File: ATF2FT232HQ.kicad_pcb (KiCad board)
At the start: 2 copper layers, 29.1 x 42.5 mm, 15 parts, among them J1 FT232HQ-Shield, J2 JTAG, SW1 SW_SPST, U1 ATF1504AS-10JU44, U2 MAX662A

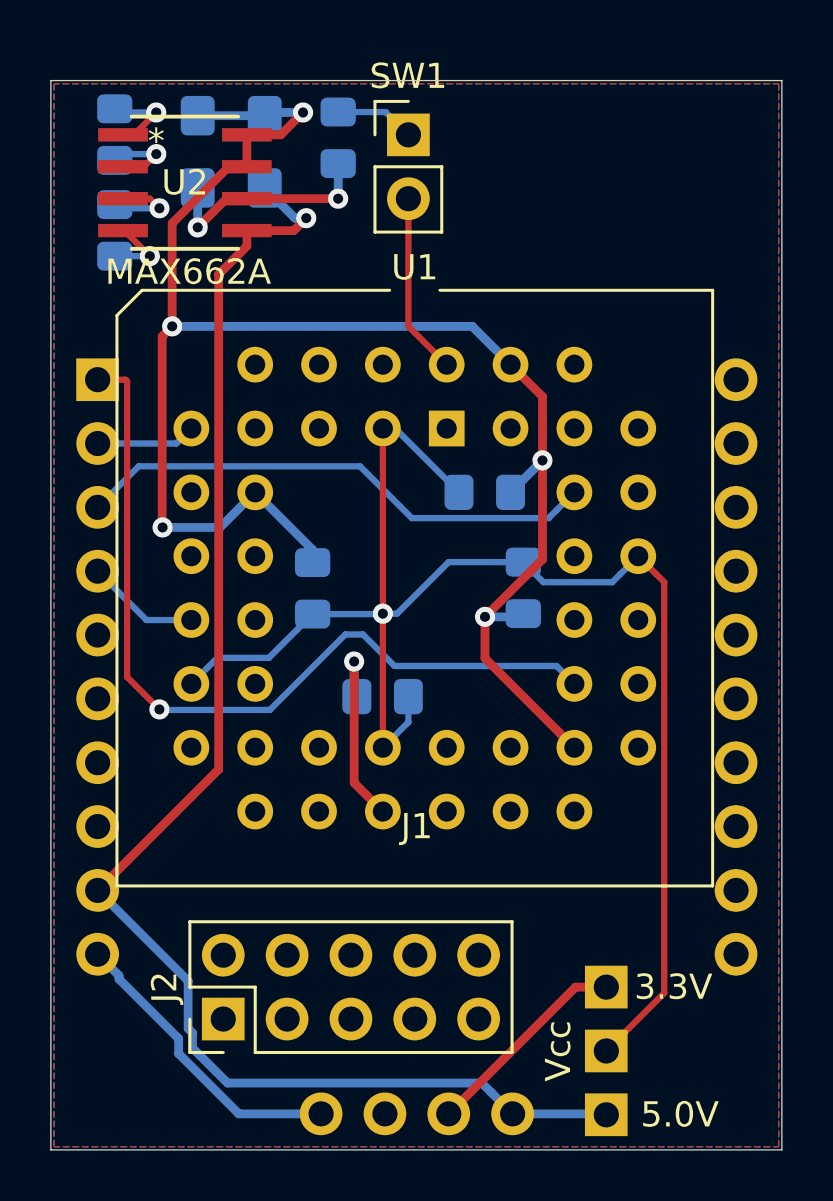
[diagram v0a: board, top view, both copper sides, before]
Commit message: First routing completed.
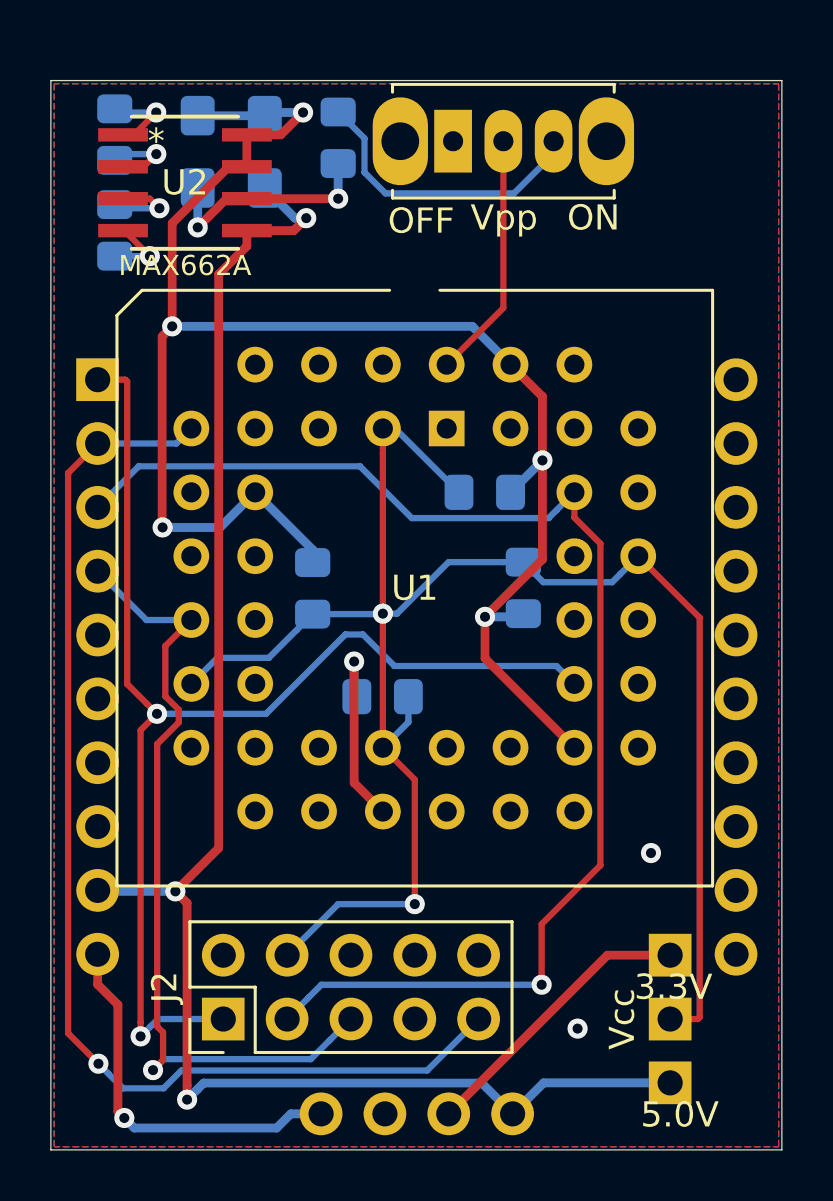
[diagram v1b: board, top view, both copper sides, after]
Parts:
- R1: value R -> 2k2
- SW1: value SW_SPST -> Vpp; footprint Connector_PinHeader_2.54mm:PinHeader_1x02_P2.54mm_Vertical -> Button_Switch_THT:SW_Slide_1P2T_CK_OS102011MS2Q
- moved JP1 2.84 mm to (180.0, 101.6)
- moved SW1 1.80 mm to (171.3, 64.1)
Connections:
- J2 pad 1: Net-(J2-Pad1) -> TCK
- J2 pad 10: Net-(J2-Pad10) -> GND
- J2 pad 2: Net-(J2-Pad2) -> GND
- J2 pad 3: Net-(J2-Pad3) -> TDO
- J2 pad 4: Net-(J2-Pad4) -> VCC
- J2 pad 5: Net-(J2-Pad5) -> TMS
- J2 pad 9: Net-(J2-Pad9) -> TDI
- SW1 pad 1: Net-(R1-Pad2) -> Net-(SW1-Pad1)
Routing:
- net TDI: track 3.98 -> 46.3 mm, vias 0 -> 1
- net TDO: track 20.9 -> 52.6 mm, vias 0 -> 1
- net TMS: track 4.53 -> 32.4 mm, vias 0 -> 1
- net TCK: track 33.4 -> 50.3 mm, vias 1 -> 2
- net VCC: track 60.9 -> 73.0 mm, vias 1 -> 2
- net Net-(R1-Pad2): track 3.17 -> 11.9 mm
- net +5V: track 58.8 -> 64.3 mm, vias 1 -> 3
- net GND: track 87.8 -> 91.0 mm, vias 6 -> 9
- net +3V3: track 8.36 -> 11.4 mm
- net Net-(SW1-Pad2): track 7.24 -> 9.82 mm
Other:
- board text added: "OFF"
- board text added: "ON"

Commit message: Moved components to the top.
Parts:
- C5, C6, C7, C8, R1: moved to F.Cu
- SW1: footprint Button_Switch_THT:SW_Slide_1P2T_CK_OS102011MS2Q -> Connector_PinHeader_2.54mm:PinHeader_1x03_P2.54mm_Vertical
- moved SW1 11.9 mm to (182.5, 68.3), turned to 180 degrees
- moved C7 7.37 mm to (168.5, 64.5)
- moved C8 7.24 mm to (171.1, 64.5)
- moved R1 6.83 mm to (173.5, 65.2)
- moved U2 2.54 mm to (163.2, 65.8)
- moved C5 0.13 mm to (158.0, 63.9)
- moved C6 0.13 mm to (158.0, 67.7)
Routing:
- net GND: track 91.0 -> 77.6 mm, vias 9 -> 8
- net Net-(SW1-Pad2): track 9.82 -> 18.5 mm, vias 0 -> 1
- net Net-(R1-Pad2): track 11.9 -> 9.38 mm
- net +5V: track 64.3 -> 66.7 mm, vias 3 -> 2
- net Net-(C6-Pad1): track 3.44 -> 2.84 mm, vias 1 -> 0
- net Net-(C5-Pad2): track 3.29 -> 2.85 mm, vias 1 -> 0
- net Net-(C6-Pad2): track 2.88 -> 3.16 mm, vias 1 -> 0
- net Net-(C5-Pad1): track 3.40 -> 3.17 mm, vias 1 -> 0
- net +12V: track 9.03 -> 9.07 mm, vias 2 -> 0
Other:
- board text added: "3.3"
- board text added: "5.0"
- board text added: "GND"
- board text added: "TCK"
- board text added: "TDI"
- board text added: "TDO"
- board text added: "TMS"
- board text added: "VCC"
- board text removed: "3.3V"
- board text removed: "5.0V"

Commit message: Labeled and tagged.
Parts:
- added G***: LOGO, Logo:bigby2, B.Cu at (157.5, 64.3)
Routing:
- net GND: track 77.6 -> 74.9 mm
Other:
- board text added: "ATF1504-FT232HQ Shield Rev.1 2019"
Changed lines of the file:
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@@
   (general
     (thickness 1.6)
-    (drawings 15)
-    (tracks 177)
+    (drawings 16)
+    (tracks 176)
     (zones 0)
-    (modules 15)
+    (modules 16)
     (nets 66)
   )
@@
     (add_net GND)
   )
+  (module Logo:bigby2 (layer B.Cu)
+    (at 157.48 64.262 180)
+    (fp_text reference G*** (at 0 0 180) (layer B.SilkS) hide
+      (effects (font (size 1.524 1.524) (thickness 0.3)) (justify mirror))
+    )
+    (fp_text value LOGO (at 0.75 0 180) (layer B.SilkS) hide
+      (effects (font (size 1.524 1.524) (thickness 0.3)) (justify mirror))
+    )
+    (fp_poly (pts (xy -0.011485 1.728467) (xy 0.113732 1.717124) (xy 0.194843 1.687923) (xy 0.241542 1.632439)
+      (xy 0.263521 1.542246) (xy 0.270474 1.408921) (xy 0.271308 1.328994) (xy 0.273257 1.04049)
+      (xy 0.168379 0.956808) (xy 0.105032 0.892095) (xy 0.067481 0.826879) (xy 0.062385 0.77734)
+      (xy 0.087312 0.759744) (xy 0.127711 0.756134) (xy 0.215607 0.74839) (xy 0.335236 0.737898)
+      (xy 0.394892 0.732679) (xy 0.531508 0.719487) (xy 0.621502 0.704831) (xy 0.681588 0.682684)
+      (xy 0.728481 0.647018) (xy 0.775892 0.595287) (xy 0.854874 0.518356) (xy 0.944952 0.451548)
+      (xy 1.029404 0.405121) (xy 1.09151 0.389332) (xy 1.105316 0.393209) (xy 1.115338 0.429014)
+      (xy 1.124376 0.514977) (xy 1.131371 0.637757) (xy 1.13502 0.76718) (xy 1.139106 0.928835)
+      (xy 1.146403 1.038611) (xy 1.158673 1.108111) (xy 1.177674 1.14894) (xy 1.195579 1.166425)
+      (xy 1.29101 1.202114) (xy 1.400648 1.196807) (xy 1.475118 1.16372) (xy 1.488952 1.150785)
+      (xy 1.500416 1.130319) (xy 1.509731 1.096728) (xy 1.517116 1.04442) (xy 1.522788 0.9678)
+      (xy 1.526969 0.861275) (xy 1.529876 0.71925) (xy 1.531729 0.536133) (xy 1.532746 0.306329)
+      (xy 1.533148 0.024245) (xy 1.533153 -0.315712) (xy 1.533153 -0.317844) (xy 1.532922 -0.658253)
+      (xy 1.532326 -0.940751) (xy 1.531144 -1.170927) (xy 1.529156 -1.354371) (xy 1.52614 -1.496672)
+      (xy 1.521875 -1.603419) (xy 1.516141 -1.680201) (xy 1.508718 -1.732606) (xy 1.499384 -1.766226)
+      (xy 1.487919 -1.786647) (xy 1.474647 -1.799064) (xy 1.376472 -1.836684) (xy 1.265456 -1.831892)
+      (xy 1.193094 -1.799607) (xy 1.175112 -1.781995) (xy 1.1613 -1.753588) (xy 1.151101 -1.706603)
+      (xy 1.14396 -1.633257) (xy 1.139323 -1.525767) (xy 1.136633 -1.37635) (xy 1.135335 -1.177223)
+      (xy 1.134934 -0.984675) (xy 1.134065 -0.211637) (xy 0.979782 -0.062148) (xy 0.901816 0.017658)
+      (xy 0.846345 0.082572) (xy 0.825499 0.118224) (xy 0.799146 0.148761) (xy 0.732681 0.189721)
+      (xy 0.696557 0.207251) (xy 0.613805 0.241662) (xy 0.55975 0.248672) (xy 0.505771 0.22821)
+      (xy 0.468235 0.206692) (xy 0.396192 0.15478) (xy 0.300546 0.073678) (xy 0.201272 -0.019618)
+      (xy 0.19561 -0.025259) (xy 0.022365 -0.198504) (xy 0.14612 -0.3024) (xy 0.221538 -0.372494)
+      (xy 0.258266 -0.434497) (xy 0.270015 -0.516179) (xy 0.270766 -0.55481) (xy 0.276486 -0.647599)
+      (xy 0.301118 -0.711947) (xy 0.35795 -0.773886) (xy 0.401734 -0.811372) (xy 0.531811 -0.919421)
+      (xy 0.518782 -1.176497) (xy 0.505754 -1.433573) (xy 0.798146 -1.702035) (xy 0.735253 -1.779705)
+      (xy 0.694397 -1.821324) (xy 0.644378 -1.844797) (xy 0.566817 -1.855141) (xy 0.450638 -1.857375)
+      (xy 0.297496 -1.851301) (xy 0.197085 -1.826154) (xy 0.139611 -1.771549) (xy 0.11528 -1.6771)
+      (xy 0.114298 -1.532418) (xy 0.115741 -1.502222) (xy 0.117859 -1.346848) (xy 0.100457 -1.238092)
+      (xy 0.056678 -1.160347) (xy -0.020335 -1.098007) (xy -0.075669 -1.066562) (xy -0.152049 -1.029637)
+      (xy -0.205195 -1.023113) (xy -0.267621 -1.046992) (xy -0.305332 -1.066562) (xy -0.402294 -1.127059)
+      (xy -0.462465 -1.194861) (xy -0.492699 -1.285576) (xy -0.499855 -1.414809) (xy -0.496742 -1.502222)
+      (xy -0.492373 -1.63025) (xy -0.497412 -1.711576) (xy -0.514532 -1.762642) (xy -0.544891 -1.798527)
+      (xy -0.615745 -1.832954) (xy -0.725524 -1.856221) (xy -0.850294 -1.866168) (xy -0.966123 -1.860635)
+      (xy -1.037737 -1.842993) (xy -1.107556 -1.793603) (xy -1.139614 -1.752578) (xy -1.150671 -1.711431)
+      (xy -1.131349 -1.666613) (xy -1.0735 -1.604152) (xy -1.029397 -1.563569) (xy -0.886666 -1.435314)
+      (xy -0.899789 -1.176378) (xy -0.912912 -0.917443) (xy -0.793004 -0.821082) (xy -0.704937 -0.7312)
+      (xy -0.659639 -0.643046) (xy -0.661706 -0.568683) (xy -0.685037 -0.537748) (xy -0.742867 -0.520353)
+      (xy -0.789634 -0.537546) (xy -0.90009 -0.569107) (xy -1.015232 -0.559689) (xy -1.107263 -0.511844)
+      (xy -1.11125 -0.508) (xy -1.157841 -0.451438) (xy -1.17475 -0.413565) (xy -1.200203 -0.379535)
+      (xy -1.262383 -0.337448) (xy -1.271377 -0.332663) (xy -1.350006 -0.274409) (xy -1.403716 -0.204314)
+      (xy -1.403829 -0.204068) (xy -1.454851 -0.13485) (xy -1.533039 -0.068093) (xy -1.545327 -0.06013)
+      (xy -1.613576 -0.004066) (xy -1.649417 0.052464) (xy -1.651 0.0635) (xy -1.649159 0.067395)
+      (xy -1.237666 0.067395) (xy -1.21517 0.004673) (xy -1.141624 -0.048336) (xy -1.062668 -0.107176)
+      (xy -1.008449 -0.17852) (xy -1.008424 -0.178574) (xy -0.954971 -0.24511) (xy -0.867178 -0.312438)
+      (xy -0.771491 -0.362989) (xy -0.705807 -0.379596) (xy -0.656443 -0.364494) (xy -0.578184 -0.324688)
+      (xy -0.53912 -0.301226) (xy -0.464733 -0.251149) (xy -0.419317 -0.214564) (xy -0.41275 -0.205286)
+      (xy -0.43488 -0.171195) (xy -0.492715 -0.108258) (xy -0.57342 -0.028572) (xy -0.664165 0.055766)
+      (xy -0.752115 0.132658) (xy -0.824438 0.190008) (xy -0.850696 0.207554) (xy -0.913247 0.241447)
+      (xy -0.961408 0.250082) (xy -1.020442 0.232418) (xy -1.094894 0.197474) (xy -1.197469 0.132211)
+      (xy -1.237666 0.067395) (xy -1.649159 0.067395) (xy -1.625844 0.116715) (xy -1.563551 0.174994)
+      (xy -1.545327 0.187131) (xy -1.465273 0.251521) (xy -1.407673 0.323668) (xy -1.40292 0.333063)
+      (xy -1.349062 0.406423) (xy -1.293916 0.446614) (xy -1.227193 0.497303) (xy -1.167951 0.573103)
+      (xy -1.167761 0.573433) (xy -1.09407 0.659684) (xy -0.986869 0.710192) (xy -0.834991 0.729664)
+      (xy -0.795652 0.730251) (xy -0.620132 0.738307) (xy -0.505713 0.762691) (xy -0.452045 0.803723)
+      (xy -0.458779 0.861724) (xy -0.525567 0.937016) (xy -0.54938 0.956808) (xy -0.654258 1.04049)
+      (xy -0.652309 1.328994) (xy -0.649069 1.485493) (xy -0.635357 1.594901) (xy -0.601479 1.665643)
+      (xy -0.537743 1.706143) (xy -0.434455 1.724827) (xy -0.281922 1.730119) (xy -0.1905 1.730375)
+      (xy -0.011485 1.728467)) (layer B.Cu) (width 0.01))
+  )
   (module max662:MAX662ACSA&plus_ (layer F.Cu)
     (at 163.195 65.786)
@@
       (rotate (xyz 0 0 0))
     )
+  )
+  (gr_text "ATF1504-FT232HQ\nShield Rev.1 2019" (at 166.624 64.008) (layer B.Cu)
+    (effects (font (size 1 1) (thickness 0.2)) (justify mirror))
   )
   (gr_text TDI (at 172.339 101.092) (layer F.SilkS)
@@
   (segment (start 161.995201 92.258799) (end 161.995201 71.971299) (width 0.35) (layer F.Cu) (net 9))
   (segment (start 161.995201 71.971299) (end 165.6588 68.3077) (width 0.35) (layer F.Cu) (net 9))
-  (segment (start 163.83 63.119) (end 161.163 63.119) (width 0.35) (layer B.Cu) (net 10))
   (via (at 160.147 71.501) (size 0.8) (drill 0.4) (layers F.Cu B.Cu) (net 10))
   (segment (start 172.085 71.501) (end 173.609 73.025) (width 0.35) (layer B.Cu) (net 10))

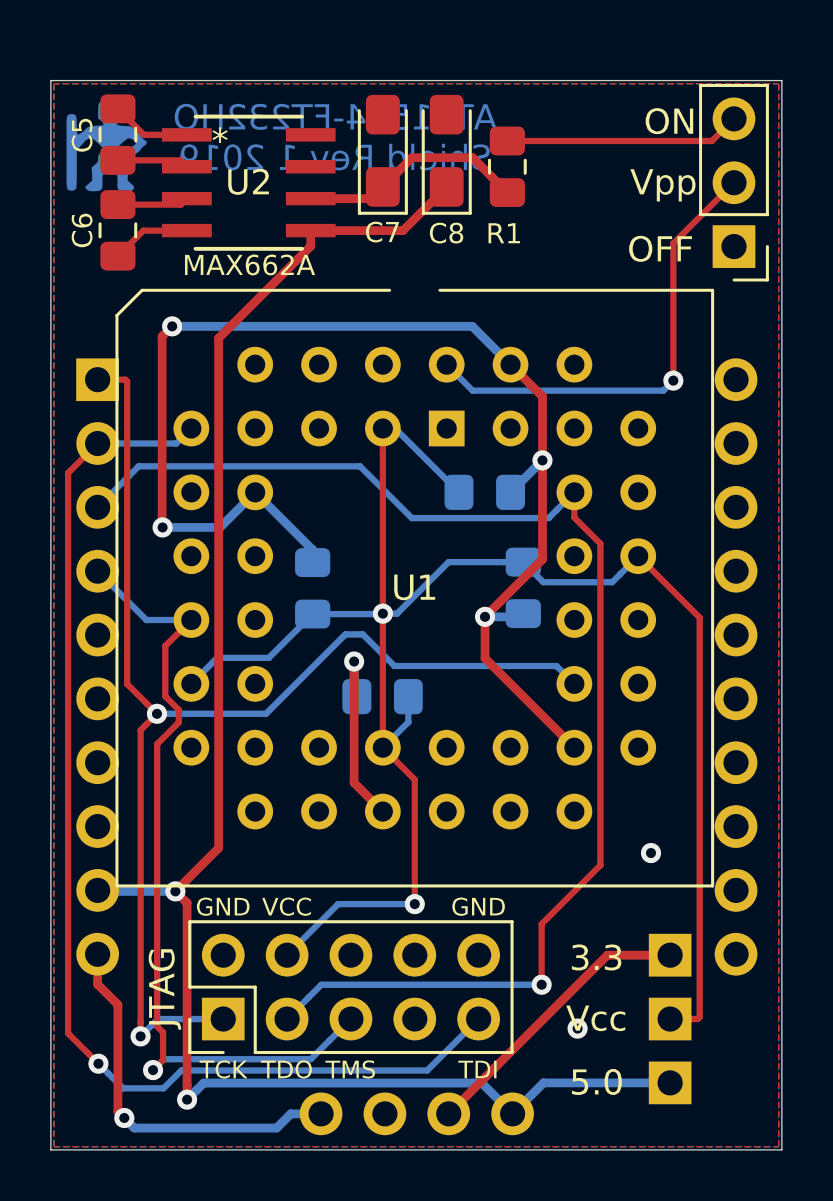
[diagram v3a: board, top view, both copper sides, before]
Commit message: Updated MAX662 footprint.
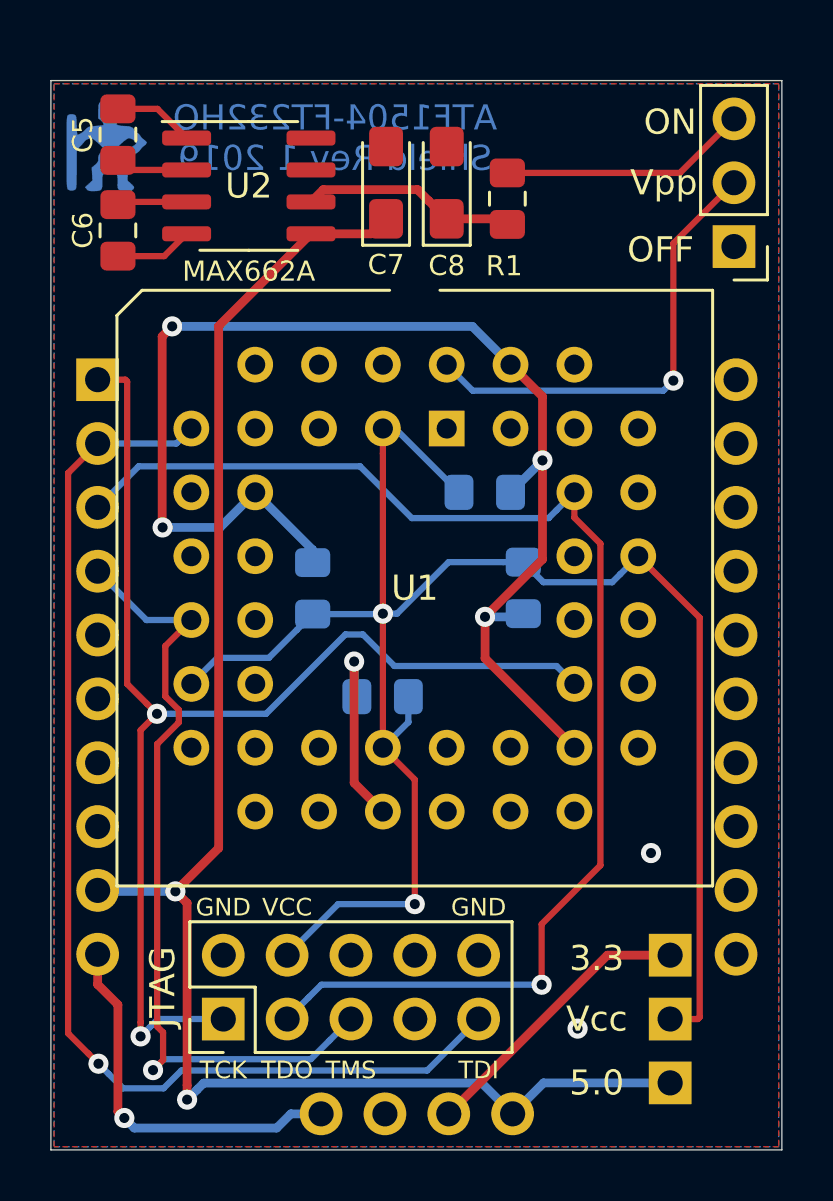
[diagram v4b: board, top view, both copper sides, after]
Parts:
- U2: footprint max662:MAX662ACSA&plus_ -> Package_SO:SOIC-8_3.9x4.9mm_P1.27mm
- moved C7 1.28 mm to (168.7, 65.8)
- moved R1 1.27 mm to (173.5, 66.4)
- moved C8 1.27 mm to (171.1, 65.8)
- moved U2 0.13 mm to (163.2, 65.9)
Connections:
- C7 pad 1: +12V -> +5V
- C8 pad 1: +5V -> +12V
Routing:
- net +5V: track 66.7 -> 63.7 mm
- net Net-(R1-Pad2): track 9.38 -> 9.91 mm
